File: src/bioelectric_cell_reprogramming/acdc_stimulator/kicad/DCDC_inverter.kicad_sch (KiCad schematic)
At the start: 17 parts, among them IC2 LTC3896EFE#PBF, Q1 IPD320N20N3GATMA1

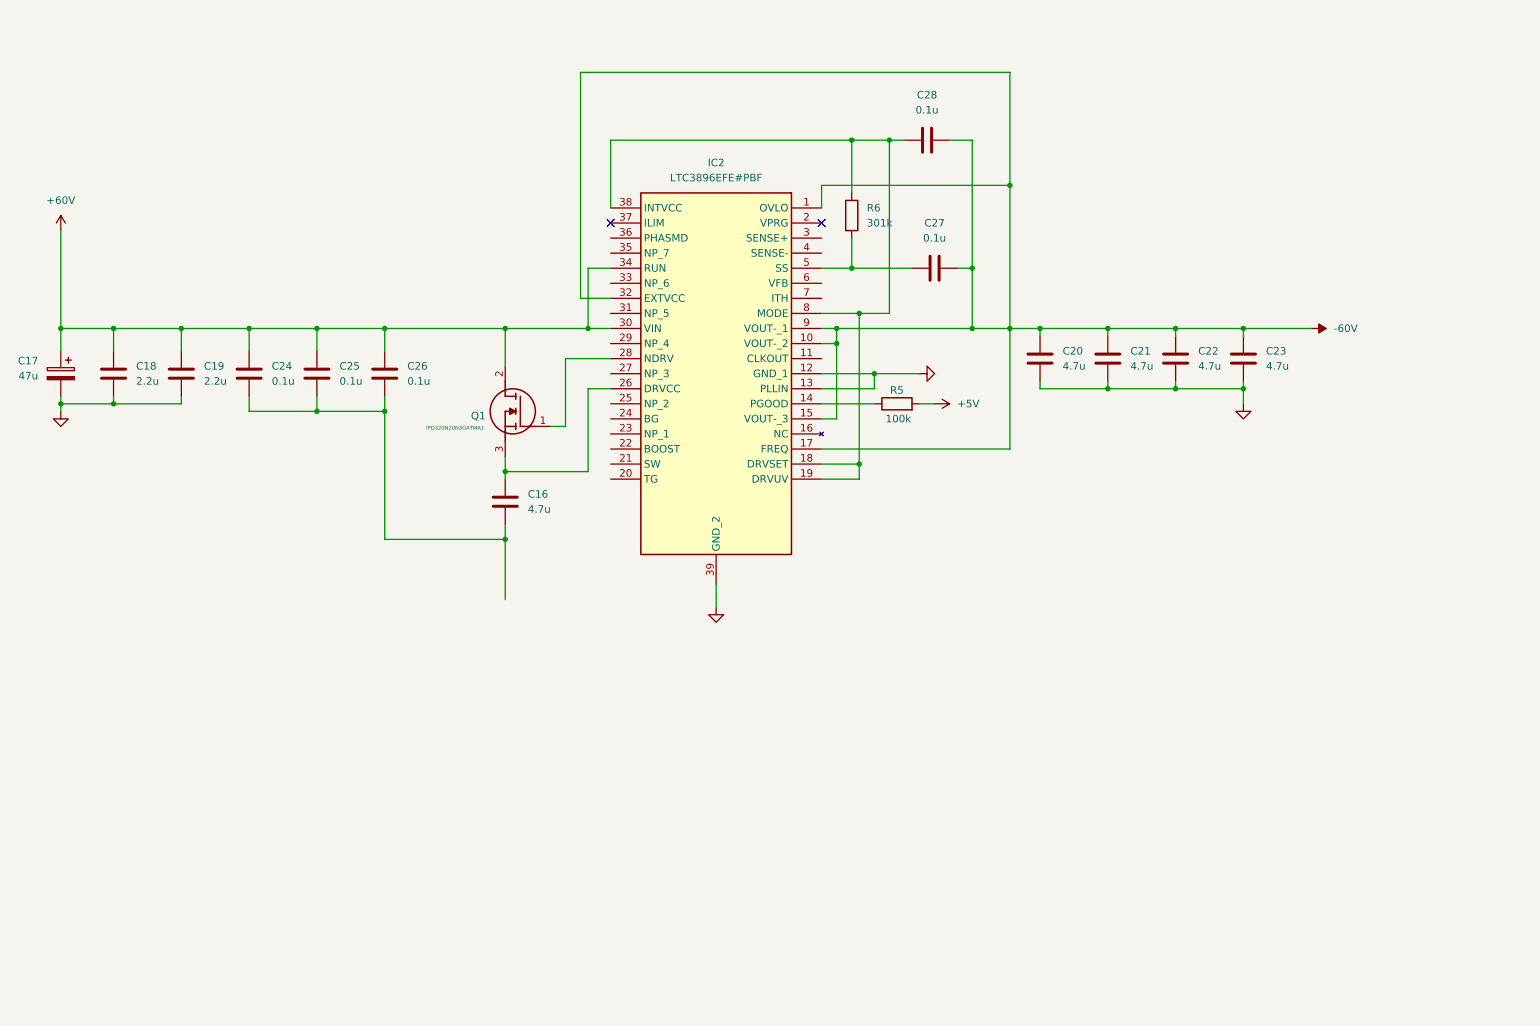
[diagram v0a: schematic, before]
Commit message: finished schematic for DC/DC inverter
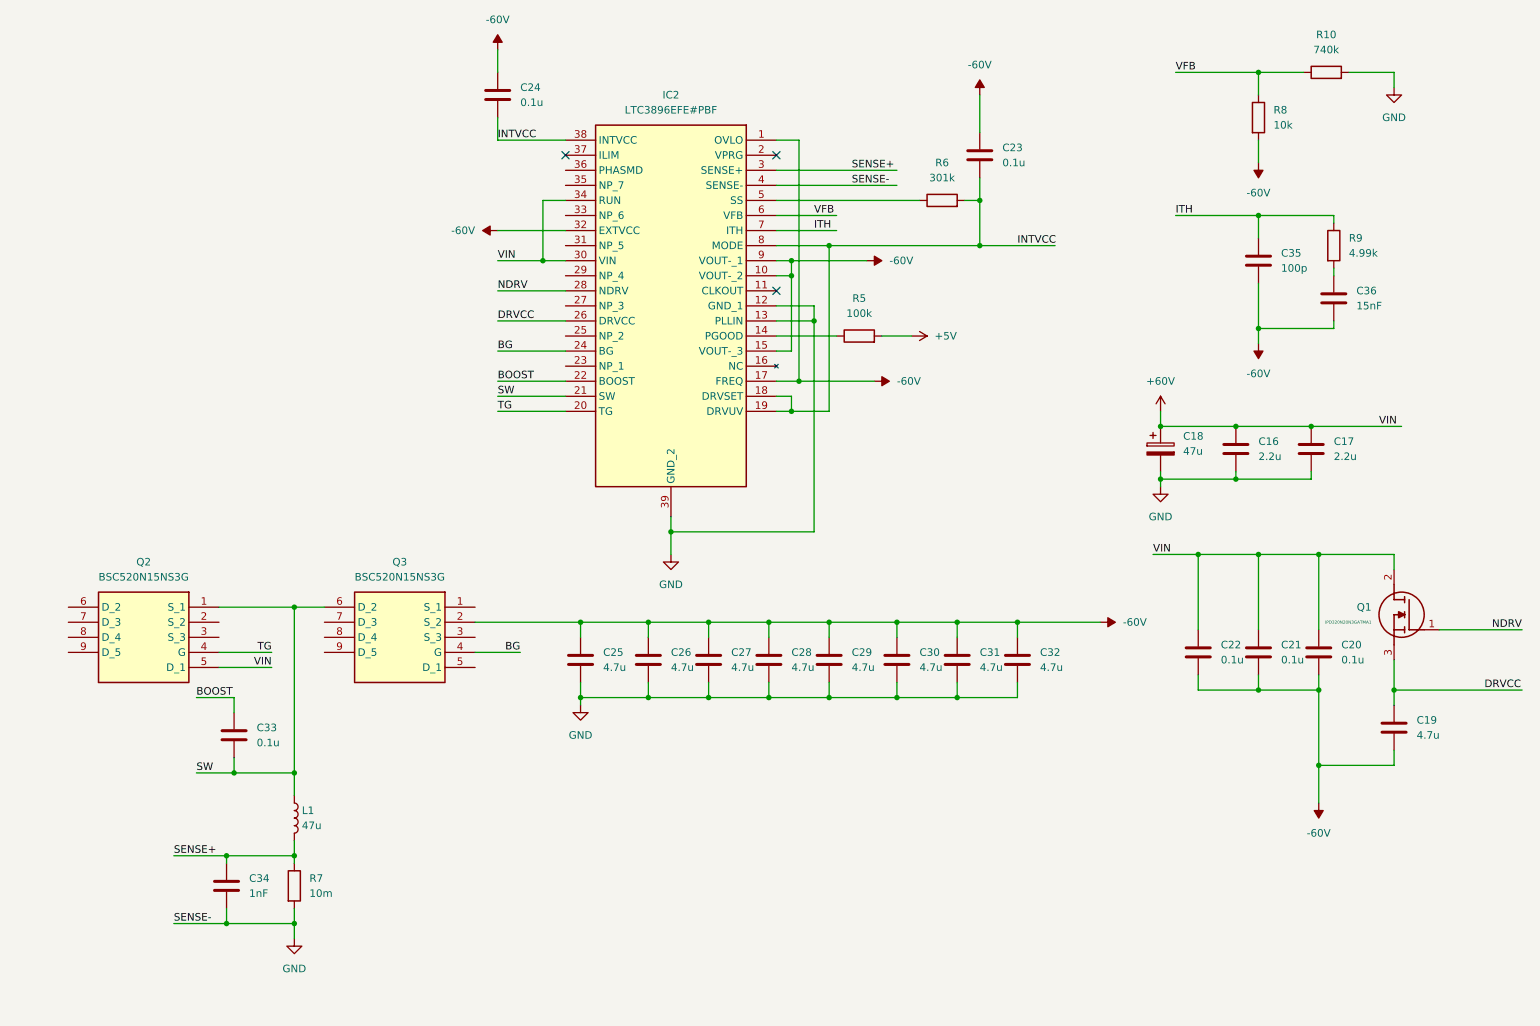
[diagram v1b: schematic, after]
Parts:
- removed C17: 47u, symbol Device:C_Polarized
- removed C18: 2.2u, symbol Device:C
- added C17: 2.2u, symbol Device:C
- added C18: 47u, symbol Device:C_Polarized
- added C29, C30, C31, C32: 4.7u, symbol Device:C
- added C33: 0.1u, symbol Device:C
- added C34: 1nF, symbol Device:C
- added C35: 100p, symbol Device:C
- added C36: 15nF, symbol Device:C
- added L1: 47u, symbol Device:L
- added Q2, Q3: BSC520N15NS3G, BSC093N04LSG, symbol BSC520N15NS3G:BSC520N15NS3G
- added R10: 740k, symbol Device:R
- added R7: 10m, symbol Device:R
- added R8: 10k, symbol Device:R
- added R9: 4.99k, symbol Device:R
- C16: value 4.7u -> 2.2u
- C19: value 2.2u -> 4.7u
- C20, C21, C22, C23: value 4.7u -> 0.1u
- C25, C26, C27, C28: value 0.1u -> 4.7u
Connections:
- net +60V: now also C16.1, C20.1, C21.1, C22.1, C17.1, C18.1, Q2.5 (D_1); no longer C19.1, C24.1, C25.1, C26.1
- net -60V: now also C19.2, C20.2, C21.2, C22.2, C24.1, C25.1, C26.1, C27.1, C28.1, C29.1, C30.1, C31.1, C32.1, C35.2, C36.2, Q3.2 (S_2), R8.2; no longer C20.1, C21.1, C22.1, C27.2, C28.2
- net GND: now also C16.2, C25.2, C26.2, C27.2, C28.2, IC2.4 (SENSE-), C17.2, C18.2, C29.2, C30.2, C31.2, C32.2, C34.2, R10.2, R7.2; no longer C19.2, C20.2, C21.2, C22.2, C23.2
- net INTVCC: now reaches IC2.18 (DRVSET), IC2.19 (DRVUV), IC2.38 (INTVCC), IC2.8 (MODE)
- net INTVCC: now also C23.2, C24.2, R6.2; no longer C28.1, R6.1
- net TG: now reaches IC2.20 (TG)
- net TG: now also Q2.4 (G)
- net SW: now reaches IC2.21 (SW)
- net SW: now also C33.2, L1.1, Q2.1 (S_1), Q3.6 (D_2)
- net BOOST: now reaches IC2.22 (BOOST)
- net BOOST: now also C33.1
- net BG: now reaches IC2.24 (BG)
- net BG: now also Q3.4 (G)
- net DRVCC: now reaches IC2.26 (DRVCC), Q1.3 (S)
- net DRVCC: now also C19.1; no longer C16.1
- net NDRV: now reaches IC2.28 (NDRV), Q1.1 (G)
- net SENSE+: now reaches IC2.3 (SENSE+)
- net SENSE+: now also C34.1, L1.2, R7.1
- net VFB: now reaches IC2.6 (VFB)
- net VFB: now also R10.1, R8.1
- net ITH: now reaches IC2.7 (ITH)
- net ITH: now also C35.1, R9.1
- new net: C36.1, R9.2
- new net: IC2.5 (SS), R6.1
- no-connect marks 2 -> 3

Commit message: ci: main AC/DC schematic done minus incubator peripherals
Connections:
- net +60V: now also Q2.6 (D_2), Q2.7 (D_3), Q2.8 (D_4), Q2.9 (D_5)
- net -60V: now also Q3.1 (S_1), Q3.3 (S_3)
- net at Q2.2 (S_2): now also Q2.3 (S_3)
- net at Q3.5 (D_1): now also Q3.7 (D_3), Q3.8 (D_4), Q3.9 (D_5)
- no-connect marks 3 -> 11
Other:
- moved on the sheet: C33, C34, L1, R7

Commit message: CI: footprint assignment done
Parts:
- removed L1: 47u, symbol Device:L
- added L1: SRR0745HA-470M, SRR0745HA-470M:SRR0745HA470M, symbol SRR0745HA-470M:SRR0745HA-470M
- C16, C17, C19, C25, C26, C27, C28, C29, C30, C31, C32: footprint (none) -> Capacitor_SMD:C_0603_1608Metric
- C18: footprint (none) -> Capacitor_THT:CP_Radial_D10.0mm_P5.00mm
- C20, C21, C22, C23, C24, C33, C35: footprint (none) -> Capacitor_SMD:C_0402_1005Metric
- C34: value 1nF -> 1n; footprint (none) -> Capacitor_SMD:C_0402_1005Metric
- C36: value 15nF -> 15n; footprint (none) -> Capacitor_SMD:C_0402_1005Metric
- IC2: footprint SOP50P640X120-39N -> LTC3896EFE#PBF:SOP50P640X120-39N
- Q1: footprint BTS3035TFATMA1 -> IPD320N20N3GATMA1:BTS3035TFATMA1
- Q2, Q3: footprint BSC093N04LSG -> BSC520N15NS3G:BSC093N04LSG
- R10, R5, R6: footprint (none) -> Resistor_SMD:R_0603_1608Metric
- R7, R8, R9: footprint (none) -> Resistor_SMD:R_0402_1005Metric
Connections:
- net SENSE+: now also L1.1
- net SW: now also L1.2
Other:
- moved on the sheet: C34, R7

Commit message: ci: STM32 layout done and schematic annotated
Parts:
- renumbered C33 to C26, C24 to C27, C34 to C28, C25 to C29, C26 to C30, C27 to C31, C28 to C32, C29 to C33, C30 to C34, C31 to C35, C23 to C36, C32 to C37, C18 to C38, C22 to C39, C16 to C40, C35 to C41, C21 to C42, C17 to C43, C20 to C44, C36 to C45, C19 to C46, IC2 to IC3, L1 to L4, Q2 to Q3, Q3 to Q4, Q1 to Q5, R7 to R16, R5 to R17, R6 to R18, R8 to R19, R10 to R20, R9 to R21

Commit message: fixed some more clearance errors
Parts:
- R19: Distributor Link (none) -> https://jlcpcb.com/partdetail/259901-NQ02WGJ0103TCE/C270371; Manufacturer (none) -> UNI-ROYAL(Uniroyal Elec); Manufacturer Part Number (none) -> NQ02WGJ0103TCE

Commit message: BOM in progress
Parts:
- C26, C27, C36, C39, C42, C44: Distributor Link (none) -> https://jlcpcb.com/partdetail/173559-GRM155R62A104KE14D/C16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; Manufacturer (none) -> Murata Electronics; Manufacturer Part Number (none) -> GRM155R62A104KE14D
- C29, C30, C31, C32, C33, C34, C35, C37, C46: footprint Capacitor_SMD:C_0603_1608Metric -> Capacitor_SMD:C_1206_3216Metric; Distributor Link (none) -> https://jlcpcb.com/partdetail/236748-GRM31CC72A475KE11L/C23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; Manufacturer (none) -> Murata Electronics; Manufacturer Part Number (none) -> GRM31CC72A475KE11L
- C40, C43: Distributor Link (none) -> https://jlcpcb.com/partdetail/3409988-GRM21BD72A225KE01L/C2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; Manufacturer (none) -> Murata Electronics; Manufacturer Part Number (none) -> GRM21BD72A225KE01L
- Q3, Q4: Distributor Link (none) -> https://jlcpcb.com/partdetail/InfineonTechnologies-BSC520N1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; Manufacturer (none) -> Infineon Technologies; Manufacturer Part Number (none) -> BSC520N15NS3G

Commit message: ci: BOM done
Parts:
- removed C28: 1n, Capacitor_SMD:C_0402_1005Metric, symbol Device:C
- added R34: 370k, Resistor_SMD:R_1206_3216Metric, symbol Device:R
- C38: footprint Capacitor_THT:CP_Radial_D10.0mm_P5.00mm -> Capacitor_SMD:CP_Elec_10x10; Distributor Link (none) -> https://jlcpcb.com/partdetail/Lelon-VEJ470M2ATR1010/C134777; Manufacturer (none) -> Lelon; Manufacturer Part Number (none) -> VEJ470M2ATR-1010
- C41: footprint Capacitor_SMD:C_0402_1005Metric -> Capacitor_SMD:C_0805_2012Metric; Distributor Link (none) -> https://jlcpcb.com/partdetail/38435-0805CG101J101NT/C37456; Manufacturer (none) -> FH (Guangdong Fenghua Advanced Tech); Manufacturer Part Number (none) -> 0805CG101J101NT
- C45: footprint Capacitor_SMD:C_0402_1005Metric -> Capacitor_SMD:C_0805_2012Metric; Distributor Link (none) -> https://jlcpcb.com/partdetail/25060-0805B153K101NT/C24320; Manufacturer (none) -> FH (Guangdong Fenghua Advanced Tech); Manufacturer Part Number (none) -> 0805B153K101NT
- IC3: Distributor Link (none) -> https://jlcpcb.com/partdetail/AnalogDevices-LTC3896EFEPBF/C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; Manufacturer (none) -> Analog Devices; Manufacturer Part Number (none) -> LTC3896EFE#PBF
- L4: Distributor Link (none) -> https://jlcpcb.com/partdetail/Bourns-SRR0745A470M/C17667599; Manufacturer (none) -> BOURNS; Manufacturer Part Number (none) -> SRR0745A-470M
- Q5: Distributor Link (none) -> https://jlcpcb.com/partdetail/InfineonTechnologies-IPD320N2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; Manufacturer (none) -> Infineon Technologies; Manufacturer Part Number (none) -> IPD320N20N3G
- R16: footprint Resistor_SMD:R_0402_1005Metric -> Resistor_SMD:R_1206_3216Metric; Distributor Link (none) -> https://jlcpcb.com/partdetail/RohmSemicon-PMR18EZPFU10L0/C3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; Manufacturer (none) -> ROHM Semicon; Manufacturer Part Number (none) -> PMR18EZPFU10L0
- R17: Distributor Link (none) -> https://jlcpcb.com/partdetail/Yageo-RC0603FR07100KL/C14675; Manufacturer (none) -> YAGEO; Manufacturer Part Number (none) -> RC0603FR-07100KL
- R18: Distributor Link (none) -> https://jlcpcb.com/partdetail/Ralec-RTT033013FTP/C103522; Manufacturer (none) -> RALEC; Manufacturer Part Number (none) -> RTT033013FTP
- R20: value 740k -> 370k; footprint Resistor_SMD:R_0603_1608Metric -> Resistor_SMD:R_1206_3216Metric; Distributor Link (none) -> https://jlcpcb.com/partdetail/Vo-SCR1206J370K/C3018094; Manufacturer (none) -> VO; Manufacturer Part Number (none) -> SCR1206J370K
- R21: Distributor Link (none) -> https://jlcpcb.com/partdetail/Koa_SpeerElec-RK73H1ETTP4991F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; Manufacturer (none) -> KOA Speer Elec; Manufacturer Part Number (none) -> RK73H1ETTP4991F
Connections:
- net GND: now also R34.2; no longer R20.2
- new net: R20.2, R34.1
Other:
- note added: "Vout = -0.8(1+R1/R2)"

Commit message: ci: fixed all relevant DRC errors with new components
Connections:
- net SW: now also Q4.5 (D_1), Q4.7 (D_3), Q4.8 (D_4), Q4.9 (D_5)
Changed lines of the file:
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@@
+	)
+	(junction
+		(at 67.31 119.38)
+		(diameter 0)
+		(color 0 0 0 0)
 	)
 	(junction
@@
 	(junction
 		(at 64.77 119.38)
+		(diameter 0)
+		(color 0 0 0 0)
+	)
+	(junction
+		(at 67.31 121.92)
 		(diameter 0)
 		(color 0 0 0 0)
@@
 	(wire
 		(pts
+			(xy 67.31 119.38) (xy 69.85 119.38)
+		)
+		(stroke
+			(width 0)
+			(type default)
+		)
+	)
+	(wire
+		(pts
 			(xy 166.37 132.08) (xy 166.37 134.62)
 		)
@@
 	(wire
 		(pts
+			(xy 67.31 119.38) (xy 67.31 121.92)
+		)
+		(stroke
+			(width 0)
+			(type default)
+		)
+	)
+	(wire
+		(pts
 			(xy 134.62 121.92) (xy 134.62 124.46)
 		)
@@
 	(wire
 		(pts
-			(xy 64.77 119.38) (xy 69.85 119.38)
-		)
-		(stroke
+			(xy 64.77 119.38) (xy 67.31 119.38)
+		)
+		(stroke
